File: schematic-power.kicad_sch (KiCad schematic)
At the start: 35 parts, among them U6 LM5013DDAR, U9 TPS62933

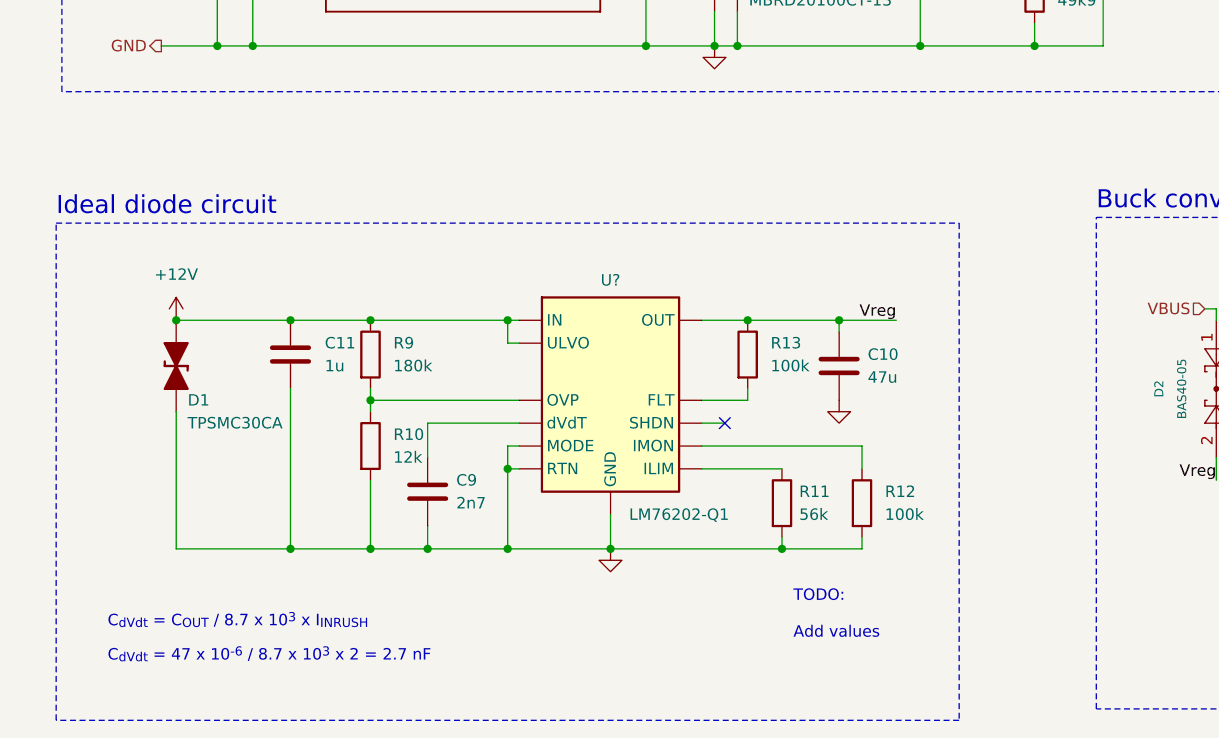
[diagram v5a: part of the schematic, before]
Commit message: Change FC connector to 10pin & ideal diode sircuit
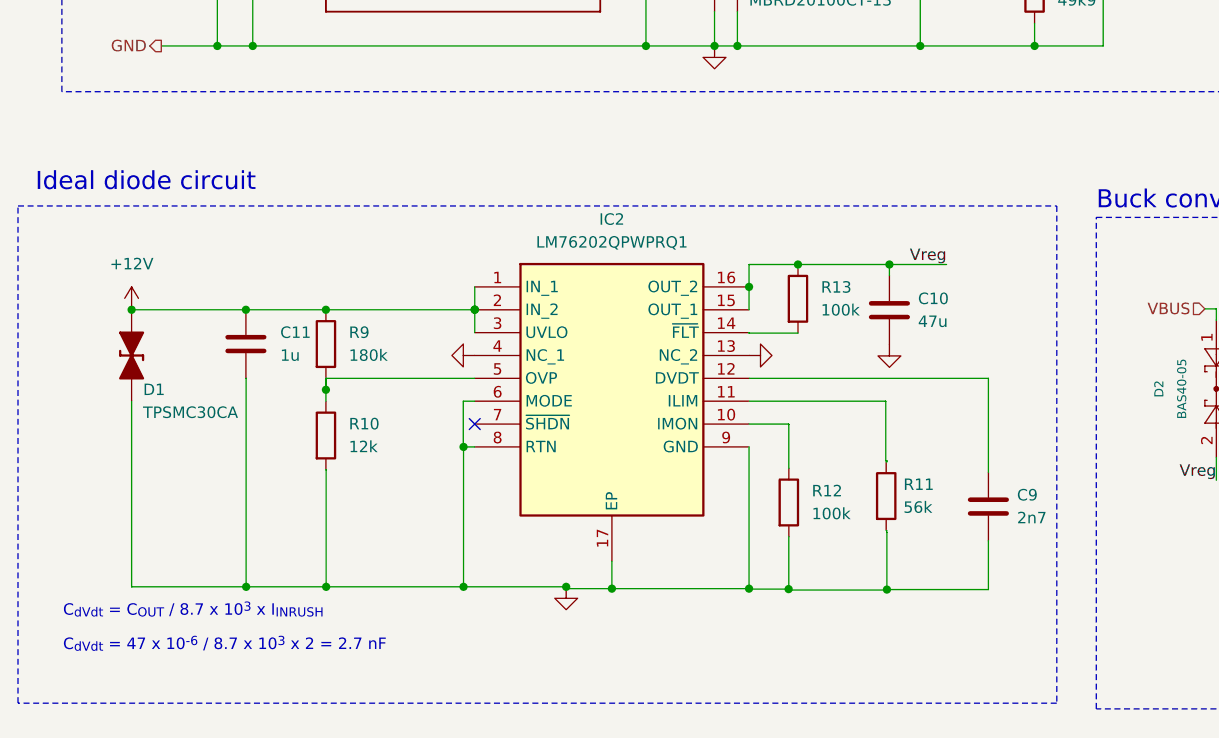
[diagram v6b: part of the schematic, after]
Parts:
- removed U?: LM76202-Q1, Package_SO:VSSOP-8_3.0x3.0mm_P0.65mm, symbol Hydros:LM76202-Q1
- added IC2: LM76202QPWPRQ1, mbr:SOP65P640X120-17N, symbol Lm7602 ideal diode:LM76202QPWPRQ1
- D1: footprint Diode_SMD_AKL:D_SMC_TVS -> lib:TPSMCSeries_LTF
- D7: footprint (none) -> MBRD20100CT-13:TO252_(DPAK)_1
- F1, F2: footprint (none) -> mbr:FUSC8664X180N
- L1: footprint Inductor_SMD:SRN3015TA4R7M -> library:SRN3015TA4R7M
- L3: footprint lib:IHLP6767DZER470M11 -> library:IHLP6767DZER470M11
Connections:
- net +12V: now also IC2.1 (IN_1), IC2.2 (IN_2), IC2.3 (UVLO)
- net GND: now also IC2.13 (NC_2), IC2.17 (EP), IC2.4 (NC_1), IC2.6 (MODE), IC2.8 (RTN), IC2.9 (GND)
- net Vreg: now also IC2.15 (OUT_1), IC2.16 (OUT_2)
- net at C9.1: now also IC2.12 (DVDT)
- net at R13.2: now also IC2.14 (~{FLT})
- net at R12.1: now also IC2.10 (IMON)
- net at R10.1, R9.2: now also IC2.5 (OVP)
- net at R11.1: now also IC2.11 (ILIM)
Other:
- note removed: "TODO: Add values"
- moved on the sheet: C10, C11, C9, D1, R10, R11, R12, R13, R9

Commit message: Complate frist version
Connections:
- net GND: no longer C17.2, R6.2, R7.1, U9.8 (FB)
- new net: C17.2, R6.2, R7.1, U9.8 (FB)
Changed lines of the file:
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@@
   (junction (at 141.097 69.85) (diameter 0) (color 0 0 0 0)
   )
+  (junction (at 77.6478 124.5616) (diameter 0) (color 0 0 0 0)
+  )
+  (junction (at 108.077 80.01) (diameter 0) (color 0 0 0 0)
+  )
+  (junction (at 54.229 45.72) (diameter 0) (color 0 0 0 0)
+  )
+  (junction (at 232.41 141.5288) (diameter 0) (color 0 0 0 0)
+  )
+  (junction (at 114.808 104.2924) (diameter 0) (color 0 0 0 0)
+  )
+  (junction (at 166.37 125.73) (diameter 0) (color 0 0 0 0)
+  )
+  (junction (at 105.537 53.34) (diameter 0) (color 0 0 0 0)
+  )
+  (junction (at 254 125.73) (diameter 0) (color 0 0 0 0)
+  )
+  (junction (at 223.52 125.73) (diameter 0) (color 0 0 0 0)
+  )
+  (junction (at 113.7666 140.3604) (diameter 0) (color 0 0 0 0)
+  )
+  (junction (at 62.357 109.3216) (diameter 0) (color 0 0 0 0)
+  )
+  (junction (at 53.4924 140.1064) (diameter 0) (color 0 0 0 0)
+  )
+  (junction (at 232.41 125.73) (diameter 0) (color 0 0 0 0)
+  )
+  (junction (at 50.292 55.88) (diameter 0) (color 0 0 0 0)
+  )
+  (junction (at 97.917 80.01) (diameter 0) (color 0 0 0 0)
+  )
+  (junction (at 128.397 80.01) (diameter 0) (color 0 0 0 0)
+  )
+  (junction (at 40.767 109.3216) (diameter 0) (color 0 0 0 0)
+  )
+  (junction (at 118.237 53.34) (diameter 0) (color 0 0 0 0)
+  )
+  (junction (at 105.537 80.01) (diameter 0) (color 0 0 0 0)
+  )
+  (junction (at 62.357 118.2116) (diameter 0) (color 0 0 0 0)
+  )
+  (junction (at 97.917 73.66) (diameter 0) (color 0 0 0 0)
+  )
+  (junction (at 141.097 80.01) (diameter 0) (color 0 0 0 0)
+  )
+  (junction (at 148.717 53.34) (diameter 0) (color 0 0 0 0)
+  )
+  (junction (at 128.397 62.23) (diameter 0) (color 0 0 0 0)
+  )
+  (junction (at 223.52 133.35) (diameter 0) (color 0 0 0 0)
+  )
+  (junction (at 53.467 109.3216) (diameter 0) (color 0 0 0 0)
+  )
+  (junction (at 141.097 53.34) (diameter 0) (color 0 0 0 0)
+  )
   (junction (at 248.92 133.35) (diameter 0) (color 0 0 0 0)
-  )
-  (junction (at 77.6478 124.5616) (diameter 0) (color 0 0 0 0)
-  )
-  (junction (at 108.077 80.01) (diameter 0) (color 0 0 0 0)
-  )
-  (junction (at 54.229 45.72) (diameter 0) (color 0 0 0 0)
-  )
-  (junction (at 114.808 104.2924) (diameter 0) (color 0 0 0 0)
-  )
-  (junction (at 166.37 125.73) (diameter 0) (color 0 0 0 0)
-  )
-  (junction (at 105.537 53.34) (diameter 0) (color 0 0 0 0)
-  )
-  (junction (at 254 125.73) (diameter 0) (color 0 0 0 0)
-  )
-  (junction (at 223.52 125.73) (diameter 0) (color 0 0 0 0)
-  )
-  (junction (at 113.7666 140.3604) (diameter 0) (color 0 0 0 0)
-  )
-  (junction (at 62.357 109.3216) (diameter 0) (color 0 0 0 0)
-  )
-  (junction (at 53.4924 140.1064) (diameter 0) (color 0 0 0 0)
-  )
-  (junction (at 232.41 125.73) (diameter 0) (color 0 0 0 0)
-  )
-  (junction (at 50.292 55.88) (diameter 0) (color 0 0 0 0)
-  )
-  (junction (at 97.917 80.01) (diameter 0) (color 0 0 0 0)
-  )
-  (junction (at 128.397 80.01) (diameter 0) (color 0 0 0 0)
-  )
-  (junction (at 40.767 109.3216) (diameter 0) (color 0 0 0 0)
-  )
-  (junction (at 118.237 53.34) (diameter 0) (color 0 0 0 0)
-  )
-  (junction (at 105.537 80.01) (diameter 0) (color 0 0 0 0)
-  )
-  (junction (at 62.357 118.2116) (diameter 0) (color 0 0 0 0)
-  )
-  (junction (at 97.917 73.66) (diameter 0) (color 0 0 0 0)
-  )
-  (junction (at 141.097 80.01) (diameter 0) (color 0 0 0 0)
-  )
-  (junction (at 148.717 53.34) (diameter 0) (color 0 0 0 0)
-  )
-  (junction (at 128.397 62.23) (diameter 0) (color 0 0 0 0)
-  )
-  (junction (at 223.52 133.35) (diameter 0) (color 0 0 0 0)
-  )
-  (junction (at 53.467 109.3216) (diameter 0) (color 0 0 0 0)
-  )
-  (junction (at 141.097 53.34) (diameter 0) (color 0 0 0 0)
   )
   (junction (at 77.6478 140.1064) (diameter 0) (color 0 0 0 0)
@@
     (stroke (width 0) (type default))
   )
-  (wire (pts (xy 232.41 133.35) (xy 248.92 133.35))
-    (stroke (width 0) (type default))
-  )
   (wire (pts (xy 124.6886 140.462) (xy 124.6886 140.4112))
     (stroke (width 0) (type default))
@@
     (stroke (width 0) (type default))
   )
+  (wire (pts (xy 248.92 133.35) (xy 248.92 141.5288))
+    (stroke (width 0) (type default))
+  )
   (wire (pts (xy 105.537 80.01) (xy 97.917 80.01))
     (stroke (width 0) (type default))
@@
     (stroke (width 0) (type default))
   )
-  (wire (pts (xy 232.41 140.97) (xy 232.41 142.113))
+  (wire (pts (xy 232.41 140.97) (xy 232.41 141.5288))
     (stroke (width 0) (type default))
   )
@@
     (stroke (width 0) (type default))
   )
+  (wire (pts (xy 232.41 141.5288) (xy 232.41 142.113))
+    (stroke (width 0) (type default))
+  )
   (wire (pts (xy 54.229 45.72) (xy 57.277 45.72))
     (stroke (width 0) (type default))
@@
     (stroke (width 0) (type default))
   )
+  (wire (pts (xy 248.92 141.5288) (xy 232.41 141.5288))
+    (stroke (width 0) (type default))
+  )

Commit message: Edit main
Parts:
- added TP1: FC test, symbol Connector:TestPoint
- D2: value BAS40-05 -> MBRD20100CT-13; footprint Package_TO_SOT_SMD:SOT-23 -> MBRD20100CT-13:TO252_(DPAK)_1
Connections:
- net SC_V: now also TP1.1
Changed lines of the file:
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@@
   (junction (at 141.097 69.85) (diameter 0) (color 0 0 0 0)
   )
+  (junction (at 50.165 45.72) (diameter 0) (color 0 0 0 0)
+  )
   (junction (at 77.6478 124.5616) (diameter 0) (color 0 0 0 0)
   )
   (junction (at 108.077 80.01) (diameter 0) (color 0 0 0 0)
   )
-  (junction (at 54.229 45.72) (diameter 0) (color 0 0 0 0)
-  )
   (junction (at 232.41 141.5288) (diameter 0) (color 0 0 0 0)
   )
@@
   )
   (junction (at 62.357 109.3216) (diameter 0) (color 0 0 0 0)
+  )
+  (junction (at 55.88 45.72) (diameter 0) (color 0 0 0 0)
   )
   (junction (at 53.4924 140.1064) (diameter 0) (color 0 0 0 0)
@@
     (stroke (width 0) (type default))
   )
-  (wire (pts (xy 50.292 45.72) (xy 54.229 45.72))
+  (wire (pts (xy 50.165 45.72) (xy 50.292 45.72))
     (stroke (width 0) (type default))
   )
@@
     (stroke (width 0) (type default))
   )
-  (wire (pts (xy 54.229 38.862) (xy 54.229 45.72))
-    (stroke (width 0) (type default))
-  )
   (wire (pts (xy 141.097 53.34) (xy 138.557 53.34))
     (stroke (width 0) (type default))
@@
     (stroke (width 0) (type default))
   )
-  (wire (pts (xy 54.229 45.72) (xy 57.277 45.72))
+  (wire (pts (xy 50.292 45.72) (xy 55.88 45.72))
     (stroke (width 0) (type default))
   )
@@
     (stroke (width 0) (type default))
   )
-  (wire (pts (xy 47.498 45.72) (xy 50.292 45.72))
+  (wire (pts (xy 47.498 45.72) (xy 50.165 45.72))
     (stroke (width 0) (type default))
   )
@@
   )
   (wire (pts (xy 40.767 109.3216) (xy 53.467 109.3216))
+    (stroke (width 0) (type default))
+  )
+  (wire (pts (xy 55.88 37.465) (xy 55.88 45.72))
+    (stroke (width 0) (type default))
+  )
+  (wire (pts (xy 55.88 45.72) (xy 57.277 45.72))
     (stroke (width 0) (type default))
   )
@@
     (effects (font (size 1.27 1.27)) (justify left))
   )
-  (hierarchical_label "SC_V" (shape output) (at 54.229 38.862 90) (fields_autoplaced)
+  (hierarchical_label "SC_V" (shape output) (at 55.88 37.465 90) (fields_autoplaced)
     (effects (font (size 1.27 1.27)) (justify left))
   )
@@
         (path "/c9ad7189-d3b2-414a-9743-efd8e57cd755/ed70203f-44bf-4bdc-8b45-a710eb8fc309"
           (reference "C4") (unit 1)
+        )
+      )
+    )
+  )
+  (symbol (lib_id "Connector:TestPoint") (at 50.165 45.72 0) (unit 1)
+    (in_bom yes) (on_board yes) (dnp no)
+    (property "Reference" "TP1" (at 50.165 36.83 0)
+      (effects (font (size 1.27 1.27)))
+    )
+    (property "Value" "FC test" (at 50.165 39.37 0)
+      (effects (font (size 1.27 1.27)))
+    )
+    (property "Footprint" "" (at 55.245 45.72 0)
+      (effects (font (size 1.27 1.27)) hide)
+    )
+    (property "Datasheet" "~" (at 55.245 45.72 0)
+      (effects (font (size 1.27 1.27)) hide)
+    )
+    (pin "1")
+    (instances
+      (project "schematic-main"
+        (path "/c9ad7189-d3b2-414a-9743-efd8e57cd755/e4695f4d-6fa6-4597-a598-6a2f28a255eb"
+          (reference "TP1") (unit 1)
+        )
+        (path "/c9ad7189-d3b2-414a-9743-efd8e57cd755/ed70203f-44bf-4bdc-8b45-a710eb8fc309"
+          (reference "TP13") (unit 1)
         )
       )
@@
       (effects (font (size 1 1)))
     )
-    (property "Value" "BAS40-05" (at 157.48 118.11 0)
+    (property "Value" "MBRD20100CT-13" (at 157.48 118.11 0)
       (effects (font (size 1 1)))
     )
-    (property "Footprint" "Package_TO_SOT_SMD:SOT-23" (at 156.21 111.76 0)
+    (property "Footprint" "MBRD20100CT-13:TO252_(DPAK)_1" (at 156.21 111.76 0)
       (effects (font (size 1.27 1.27)) (justify left) hide)
     )
